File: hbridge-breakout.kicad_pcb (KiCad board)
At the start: 2 copper layers, 28.5 x 38.6 mm, 15 parts, among them J1 Conn_01x10, J2 Conn_01x04, J3 Conn_01x08, U1 74HC00, U2 DRV8870DDA

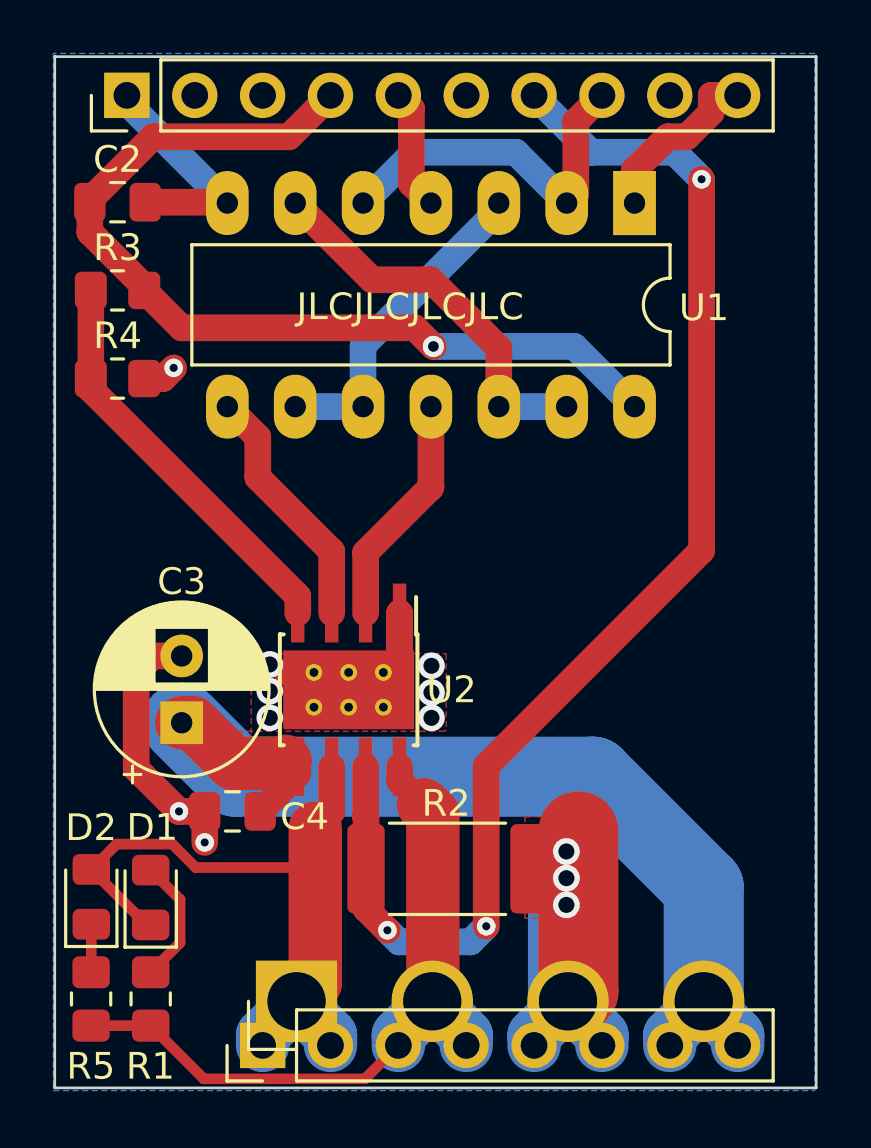
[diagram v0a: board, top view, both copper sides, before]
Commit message: Fixed a terrible bug where the power input/outputs at the bottom of the board were flipped.
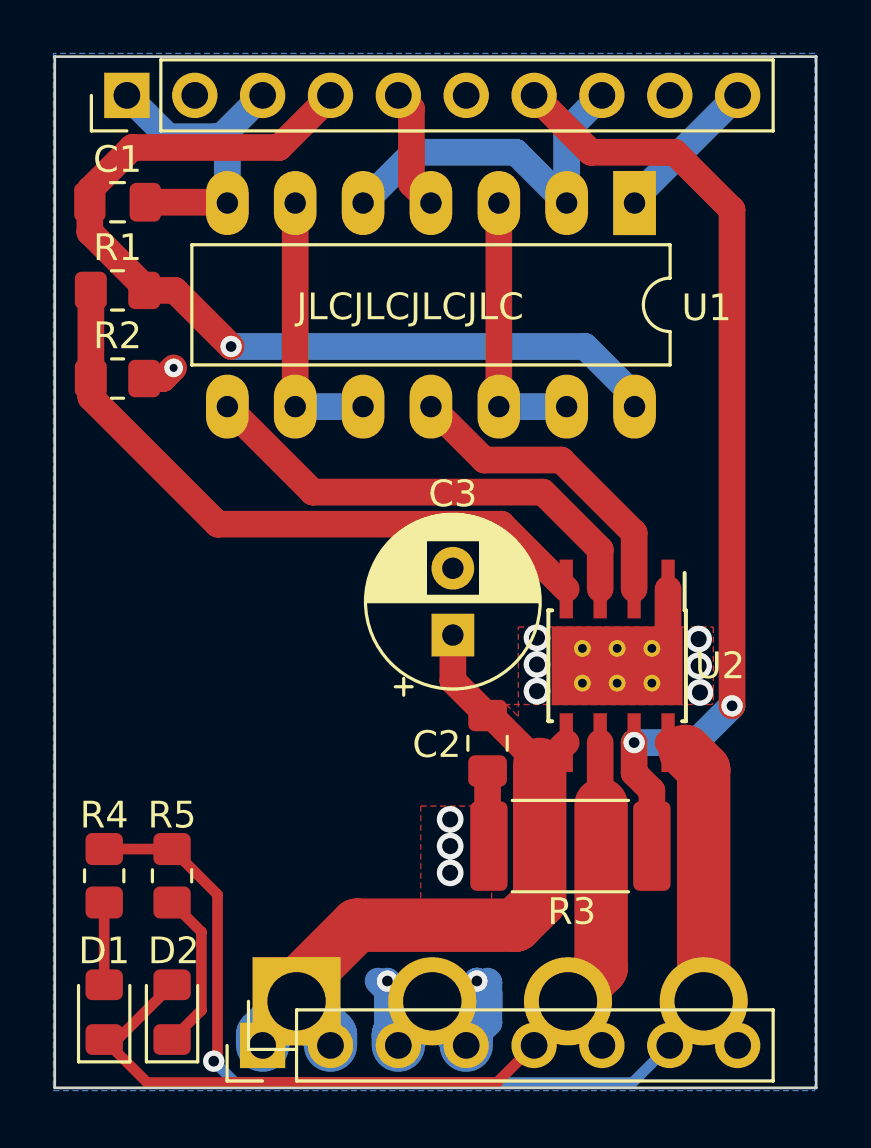
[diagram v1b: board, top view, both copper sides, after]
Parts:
- R1: renamed from R3; value R -> 10k
- R2: renamed from R4; value R -> 20k
- R4: renamed from R5; value 4k7 -> 2k
- R5: renamed from R1; value 4k7 -> 18k
- moved C3 10.7 mm to (165.4, 97.4)
- moved U2 10.1 mm to (171.6, 98.5)
- moved C2 9.88 mm to (166.8, 101.5), turned to -90 degrees
- moved R5 4.68 mm to (154.9, 106.4)
- moved R3 4.68 mm to (169.8, 105.3), turned to 180 degrees
- moved R4 4.64 mm to (152.4, 106.4)
- moved D2 4.37 mm to (154.9, 111.5)
- moved D1 4.34 mm to (152.4, 111.5)
- renumbered C2 to C1, C4 to C2, D2 to D1, D1 to D2, R2 to R3
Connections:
- D1 pad 1: Net-(D2-K) -> /OUTB
- D1 pad 2: /OUTA -> Net-(D1-A)
- D2 pad 1: /OUTA -> Net-(D2-K)
- D2 pad 2: Net-(D1-A) -> /OUTB
- J1 pad 3: unconnected-(J1-Pin_3-Pad3) -> GND
- J2 pad 1: /OUTA -> VCC
- J2 pad 2: /OUTB -> GND
- J2 pad 3: GND -> /OUTB
- J2 pad 4: VCC -> /OUTA
- J3 pad 1: /OUTA -> VCC
- J3 pad 2: /OUTA -> VCC
- J3 pad 3: /OUTB -> GND
- J3 pad 4: /OUTB -> GND
- J3 pad 5: GND -> /OUTB
- J3 pad 6: GND -> /OUTB
- J3 pad 7: VCC -> /OUTA
- J3 pad 8: VCC -> /OUTA
- R4 pad 1: Net-(D2-K) -> /OUTA
- R4 pad 2: /OUTB -> Net-(D1-A)
- R5 pad 1: Net-(D1-A) -> /OUTA
- R5 pad 2: /OUTB -> Net-(D2-K)
- U1 pad 3: Net-(U1-Pad10) -> Net-(U1-Pad12)
- U1 pad 6: Net-(U1-Pad12) -> Net-(U1-Pad10)
- U2 pad 6: /OUTA -> /OUTB
- U2 pad 8: /OUTB -> /OUTA
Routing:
- net /OUTA: track 25.9 -> 39.6 mm, vias 0 -> 1
- net /CS: track 49.5 -> 36.1 mm, vias 3 -> 2
- net GND: track 44.4 -> 34.8 mm
- net Net-(U2-VREF): track 15.3 -> 24.8 mm
- net VCC: track 37.5 -> 28.0 mm
- net /IN1: track 9.34 -> 17.6 mm
- net Net-(U1-Pad12): track 14.6 -> 10.2 mm
- net /OUTB: track 26.5 -> 30.9 mm
- net Net-(D2-K): track 1.80 -> 6.04 mm
- net /IN2: track 8.74 -> 11.7 mm
- net Net-(U1-Pad10): track 12.3 -> 10.2 mm
- net Net-(D1-A): track 4.73 -> 3.08 mm
- net /INA: track 6.63 -> 5.63 mm
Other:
- board text added: "mjd 2.0a 18-Apr-24"
- board text removed: "mjd 1.2a 19-Sep-23"
